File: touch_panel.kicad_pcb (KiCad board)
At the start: 2 copper layers, 50 x 50 mm, 46 parts, among them J1 2x4 SMD 2.0 MM, J2 2x4 Regular, Q1 MMBT2222, Q2 MMBT2222, Q3 MMBT2222, Q4 MMBT2222, Q5 MMBT2222, Q6 MMBT2222, SW1 Reset Switch, U1 TTP223_1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

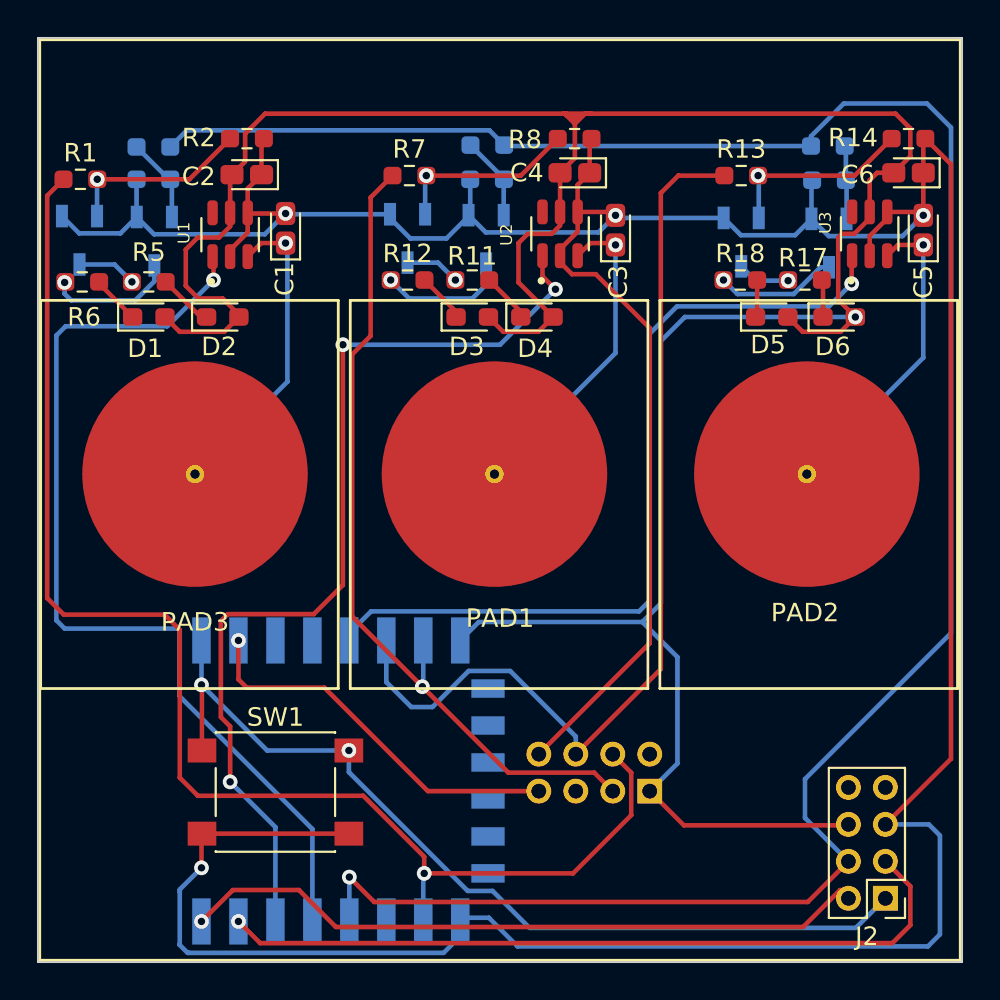
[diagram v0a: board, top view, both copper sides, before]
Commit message: Some routes updated for better cut
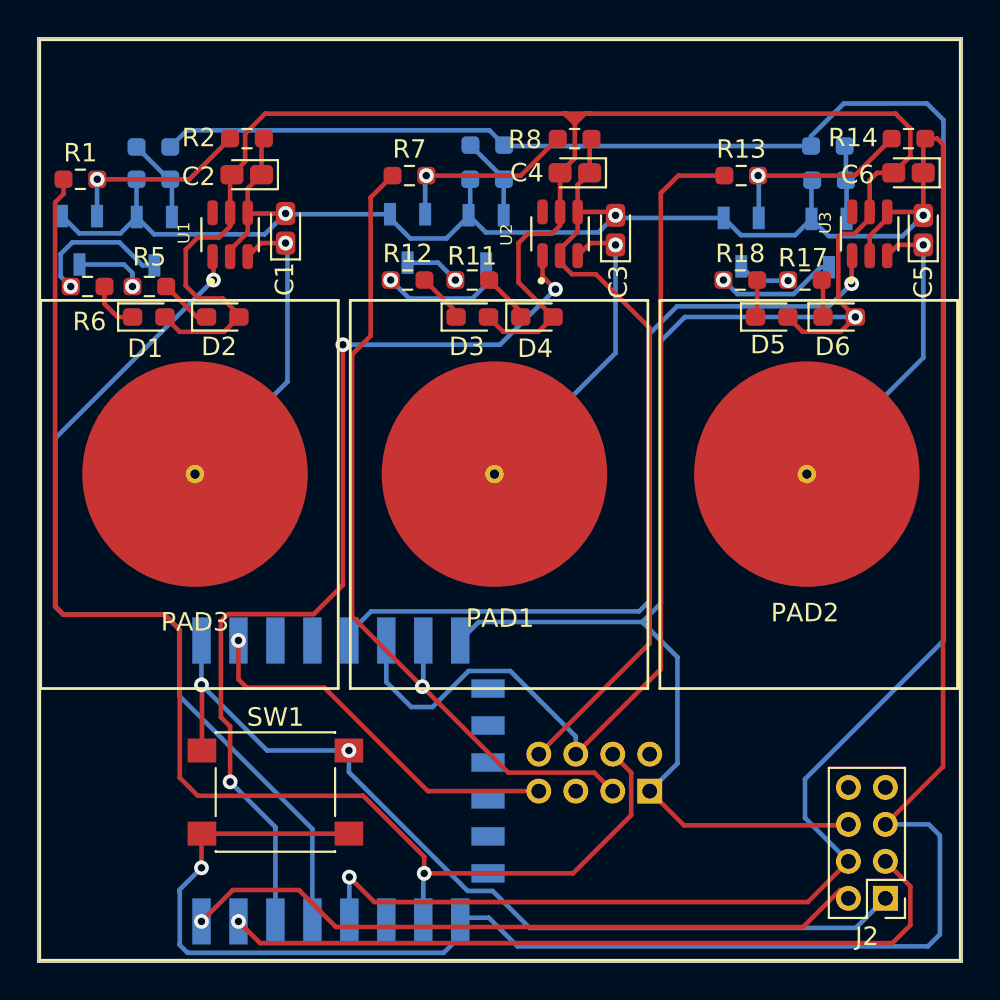
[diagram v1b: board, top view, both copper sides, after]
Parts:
- moved R6 0.38 mm to (110.2, 92.8)
- moved R5 0.25 mm to (113.5, 92.8)
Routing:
- net Touch 1: track 52.1 -> 48.5 mm
- net Net-(Q2-Pad3): track 6.90 -> 7.83 mm
- net Net-(Q1-Pad3): track 3.42 -> 3.98 mm
